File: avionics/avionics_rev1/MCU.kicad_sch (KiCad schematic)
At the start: 13 parts, among them U2 STM32G474RETx

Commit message: saving work before chat
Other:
- note added: "TODO: pins for SPI / I2C devices pins for buzzer / status LED(s) pins for pyro channels pins for battery monitoring / current draw determine if this needs a crystal or not (prolly) pins for USB connections pins for debug header"
- note removed: "TODO: pins for SPI / I2C devices pins for buzzer / status LED(s) pins for pyro channels pins for battery monitoring / current draw"
- moved on the sheet: C10, C11, C14, C6, C7, C8, C9, FB1

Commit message: working on sensors schematics
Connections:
- net VREF: no longer FB2.2, U2.28 (VREF+)
- new net: FB2.2, U2.28 (VREF+)
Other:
- note added: "TODO: determine pins for SPI / I2C devices determine pins for buzzer / status LED(s) determine pins for pyro channels determine pins for battery monitoring / current draw (find IC for current sensing) determine if this needs a crystal or not (probably) determine pins for USB connections determine pins for other telemetry IO setup a debug header / look into STlink find a flash memory chip and wire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"
- note removed: "TODO: pins for SPI / I2C devices pins for buzzer / status LED(s) pins for pyro channels pins for battery monitoring / current draw determine if this needs a crystal or not (prolly) pins for USB connections pins for debug header"
- moved on the sheet: BZ1, C14

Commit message: saving MCU work before using codex
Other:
- note added: "TODO: determine pins for SPI / I2C (if any) devices determine pins for buzzer / status LED(s) determine pins for pyro channels determine pins for battery monitoring / current draw (find IC for current sensing) determine if this needs a crystal or not (probably) determine pins for USB connections determine pins for other telemetry IO setup a debug header / look into STlink find a flash memory chip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"
- note removed: "TODO: determine pins for SPI / I2C devices determine pins for buzzer / status LED(s) determine pins for pyro channels determine pins for battery monitoring / current draw (find IC for current sensing) determine if this needs a crystal or not (probably) determine pins for USB connections determine pins for other telemetry IO setup a debug header / look into STlink find a flash memory chip and wire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"
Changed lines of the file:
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@@
 	(generator "eeschema")
 	(generator_version "10.0")
-	(paper "A4")
+	(paper "A3")
 	(text "Reference the Nucleo64 STM32G4 board\nfor this power layout"
 		(exclude_from_sim no)
@@
 		)
 	)
-	(text "TODO: \ndetermine pins for SPI / I2C devices\ndetermine pins for buzzer / status LED(s)\ndetermine pins for pyro channels\ndetermine pins for battery monitoring / \ncurrent draw (find IC for current sensing)\ndetermine if this needs a crystal or not (probably)\ndetermine pins for USB connections\ndetermine pins for other telemetry IO\nsetup a debug header / look into STlink\nfind a flash memory chip and wire it up"
+	(text "TODO: \ndetermine pins for SPI / I2C (if any) devices\ndetermine pins for buzzer / status LED(s)\ndetermine pins for pyro channels\ndetermine pins for battery monitoring / \ncurrent draw (find IC for current sensing)\ndetermine if this needs a crystal or not (probably)\ndetermine pins for USB connections\ndetermine pins for other telemetry IO\nsetup a debug header / look into STlink\nfind a flash memory chip and wire it up (needs to hold flight data)\nconnect existing flags to corresponding pins\nadd voltages/tolerances for capacitors/resistors"
 		(exclude_from_sim no)
-		(at 20.32 40.894 0)
+		(at 214.63 122.936 0)
 		(effects
 			(font

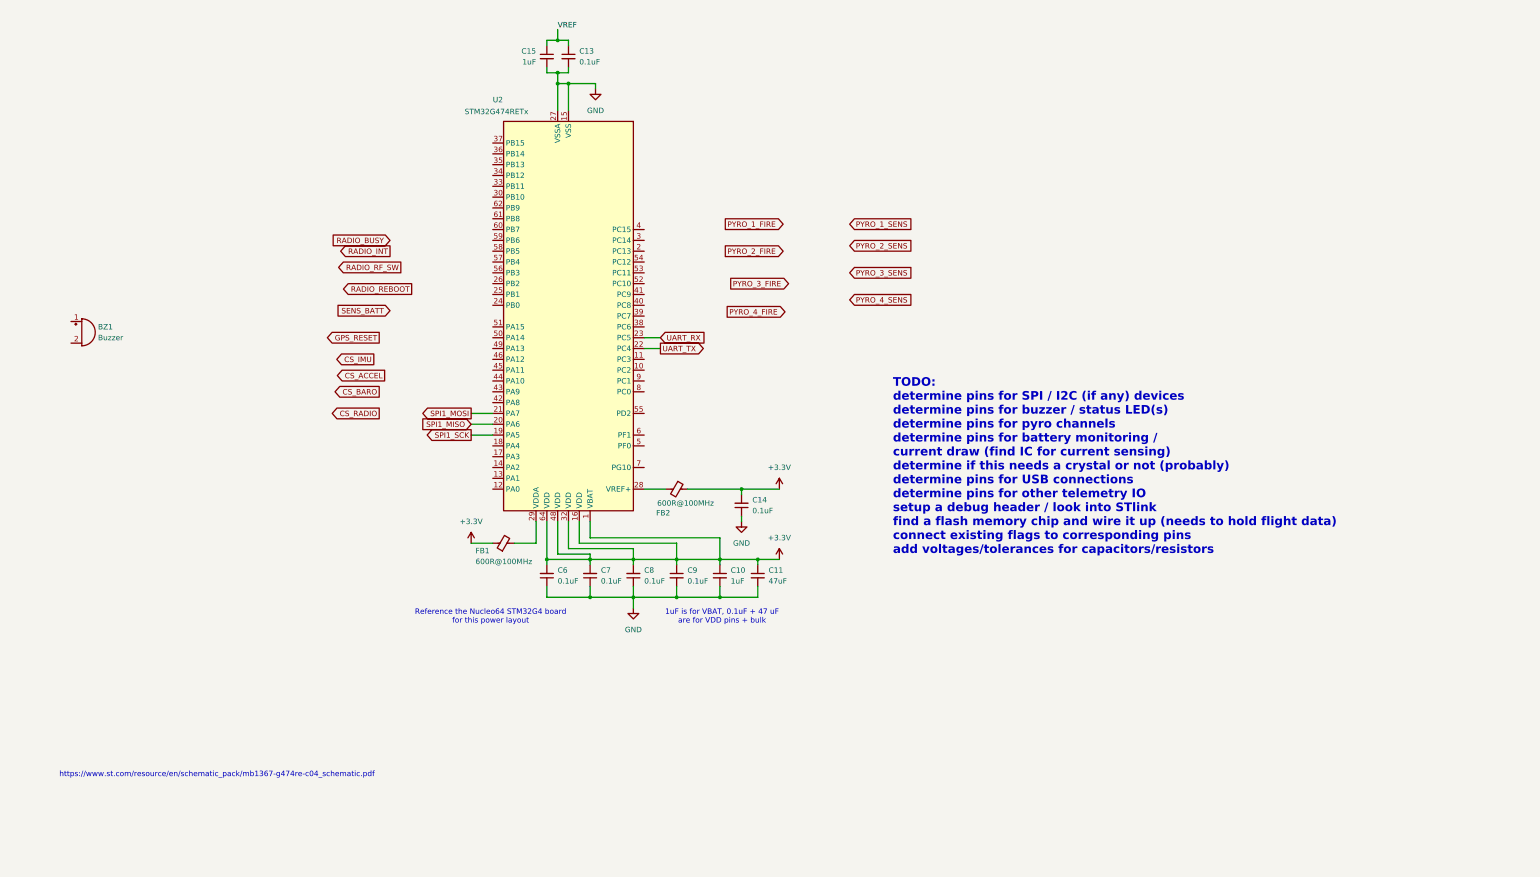
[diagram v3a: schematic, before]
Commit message: cleaned up schematics after codex work
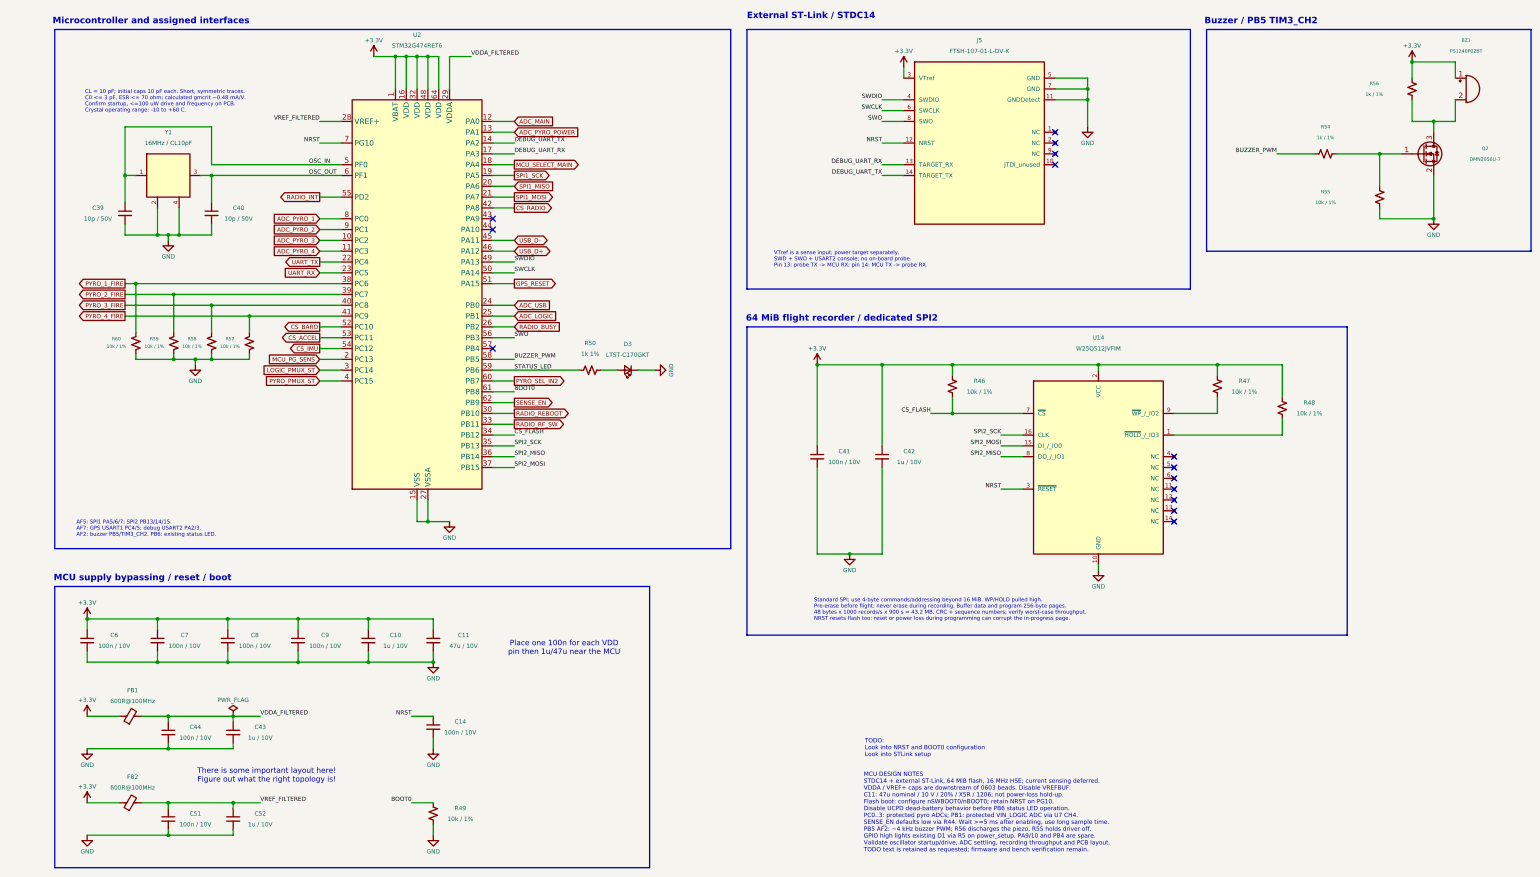
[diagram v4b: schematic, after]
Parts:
- removed BZ1: Buzzer, avionics_footprints:XDCR_PS1240P02BT, symbol Device:Buzzer
- removed C13: 0.1uF, Capacitor_SMD:C_0201_0603Metric, symbol Device:C_Small
- removed C15: 1uF, Capacitor_SMD:C_0201_0603Metric, symbol Device:C_Small
- removed FB2: 600R@100MHz, Capacitor_SMD:C_0201_0603Metric, symbol Device:FerriteBead_Small
- added BZ1: PS1240P02BT, avionics_footprints:XDCR_PS1240P02BT, symbol rocketry_library:PS1240P02BT
- added C39, C40: 10p / 50V, Capacitor_SMD:C_0402_1005Metric, symbol rocketry_library:C0402C100J5GACTU
- added C41, C44, C51: 100n / 10V, Capacitor_SMD:C_0402_1005Metric, symbol rocketry_library:GRM155R71A104KA01D
- added C42, C43, C52: 1u / 10V, Capacitor_SMD:C_0603_1608Metric, symbol rocketry_library:C1608X7R1A105K080AC
- added D3: LTST-C170GKT, avionics_footprints:LTST_C170GKT_0805, symbol Device:LED_Small
- added FB2: 600R@100MHz, Inductor_SMD:L_0603_1608Metric, symbol rocketry_library:BLM18AG601SN1D
- added J5: FTSH-107-01-L-DV-K, avionics_footprints:FTSH-107-01-L-DV-K_STDC14, symbol rocketry_library:FTSH-107-01-L-DV-K_STDC14
- added Q2: DMN2056U-7, avionics_footprints:DMN2056U_7_SOT23, symbol rocketry_library:DMN2056U-7
- added R46, R47, R48, R49, R55, R57, R58, R59, R60: 10k / 1%, Resistor_SMD:R_0402_1005Metric, symbol rocketry_library:RC0402FR-0710KL
- added R50: 1k 1%, Resistor_SMD:R_0402_1005Metri, symbol rocketry_library:RC0402FR-071KL
- added R54, R56: 1k / 1%, Resistor_SMD:R_0402_1005Metric, symbol rocketry_library:RC0402FR-071KL
- added U14: W25Q512JVFIM, avionics_footprints:W25Q512JVFIM_SOIC16W, symbol rocketry_library:W25Q512JVFIM
- added Y1: 16MHz / CL10pF, avionics_footprints:ABM8_3.2x2.5mm, symbol rocketry_library:ABM8-16.000MHZ-10-1-U-T
- C10: value 1uF -> 1u / 10V; footprint Capacitor_SMD:C_0201_0603Metric -> Capacitor_SMD:C_0603_1608Metric; symbol Device:C_Small -> rocketry_library:C1608X7R1A105K080AC; Dielectric (none) -> X7R; DigiKey (none) -> https://www.digikey.com/en/products/detail/tdk/C1608X7R1A10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; MPN (none) -> C1608X7R1A105K080AC; Tolerance (none) -> 10%; Voltage (none) -> 10V
- C11: value 47uF -> 47u / 10V; footprint Capacitor_SMD:C_0201_0603Metric -> Capacitor_SMD:C_1206_3216Metric; symbol Device:C_Small -> rocketry_library:C3216X5R1A476M160AB; Dielectric (none) -> X5R; DigiKey (none) -> https://www.digikey.com/en/products/detail/tdk/C3216X5R1A47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; MPN (none) -> C3216X5R1A476M160AB; Tolerance (none) -> 20%; Voltage (none) -> 10V
- C14, C6, C7, C8, C9: value 0.1uF -> 100n / 10V; footprint Capacitor_SMD:C_0201_0603Metric -> Capacitor_SMD:C_0402_1005Metric; symbol Device:C_Small -> rocketry_library:GRM155R71A104KA01D; Dielectric (none) -> X7R; DigiKey (none) -> https://www.digikey.com/en/products/detail/murata-electroni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; MPN (none) -> GRM155R71A104KA01D; Tolerance (none) -> 10%; Voltage (none) -> 10V
- FB1: footprint Capacitor_SMD:C_0201_0603Metric -> Inductor_SMD:L_0603_1608Metric; symbol Device:FerriteBead_Small -> rocketry_library:BLM18AG601SN1D; DigiKey (none) -> https://www.digikey.com/en/products/detail/murata-electroni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; Impedance tolerance (none) -> 25%; MPN (none) -> BLM18AG601SN1D
- U2: value STM32G474RETx -> STM32G474RET6; symbol MCU_ST_STM32G4:STM32G474RETx -> rocketry_library:STM32G474RET6
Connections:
- net +3.3V: now also C6.1, C7.1, C8.1, BZ1.1 (+), C41.1, C42.1, FB2.1, J5.3 (VTref), R46.1, R47.1, R48.1, R56.1, U14.2 (VCC); no longer C14.2, C6.2, C7.2, C8.2
- net CS_ACCEL: now also U2.53 (PC11)
- net CS_BARO: now also U2.52 (PC10)
- net CS_IMU: now also U2.54 (PC12)
- net CS_RADIO: now also U2.42 (PA8)
- net GND: now also C14.2, C6.2, C7.2, C8.2, C39.2, C40.2, C41.2, C42.2, C43.2, C44.2, C51.2, C52.2, D3.1 (K), J5.11 (GNDDetect), J5.5 (GND), J5.7 (GND), Q2.2 (S), R49.2, R55.2, R57.2, R58.2, R59.2, R60.2, U14.10 (GND), Y1.2 (CASE), Y1.4 (CASE); no longer C14.1, C6.1, C7.1, C8.1
- net GPS_RESET: now also U2.51 (PA15)
- net PYRO_1_FIRE: now also U2.38 (PC6), R60.1
- net PYRO_2_FIRE: now also U2.39 (PC7), R59.1
- net PYRO_3_FIRE: now also U2.40 (PC8), R58.1
- net PYRO_4_FIRE: now also U2.41 (PC9), R57.1
- net RADIO_BUSY: now also U2.26 (PB2)
- net RADIO_INT: now also U2.55 (PD2)
- net RADIO_REBOOT: now also U2.30 (PB10)
- net RADIO_RF_SW: now also U2.33 (PB11)
- net VDDA_FILTERED: now reaches FB1.2, U2.29 (VDDA)
- net VDDA_FILTERED: now also C43.1, C44.1
- net VREF_FILTERED: now reaches U2.28 (VREF+)
- net VREF_FILTERED: now also C51.1, C52.1, FB2.2
- net ADC_PYRO_3: now reaches U2.10 (PC2)
- net ADC_PYRO_4: now reaches U2.11 (PC3)
- net ADC_MAIN: now reaches U2.12 (PA0)
- net ADC_PYRO_POWER: now reaches U2.13 (PA1)
- net DEBUG_UART_TX: now reaches U2.14 (PA2)
- net DEBUG_UART_TX: now also J5.14 (TARGET_TX)
- net DEBUG_UART_RX: now reaches U2.17 (PA3)
- net DEBUG_UART_RX: now also J5.13 (TARGET_RX)
- net MCU_SELECT_MAIN: now reaches U2.18 (PA4)
- net MCU_PG_SENS: now reaches U2.2 (PC13)
- net ADC_USB: now reaches U2.24 (PB0)
- net ADC_LOGIC: now reaches U2.25 (PB1)
- net LOGIC_PMUX_ST: now reaches U2.3 (PC14)
- net CS_FLASH: now reaches U2.34 (PB12)
- net CS_FLASH: now also R46.2, U14.7 (~{CS})
- net SPI2_SCK: now reaches U2.35 (PB13)
- net SPI2_SCK: now also U14.16 (CLK)
- net SPI2_MISO: now reaches U2.36 (PB14)
- net SPI2_MISO: now also U14.8 (DO_/_IO1)
- net SPI2_MOSI: now reaches U2.37 (PB15)
- net SPI2_MOSI: now also U14.15 (DI_/_IO0)
- net PYRO_PMUX_ST: now reaches U2.4 (PC15)
- net USB_D-: now reaches U2.45 (PA11)
- net USB_D+: now reaches U2.46 (PA12)
- net SWDIO: now reaches U2.49 (PA13)
- net SWDIO: now also J5.4 (SWDIO)
- net OSC_IN: now reaches U2.5 (PF0)
- net OSC_IN: now also C39.1, Y1.1 (OSC1)
- net SWCLK: now reaches U2.50 (PA14)
- net SWCLK: now also J5.6 (SWCLK)
- net SWO: now reaches U2.56 (PB3)
- net SWO: now also J5.8 (SWO)
- net BUZZER_PWM: now reaches U2.58 (PB5)
- net BUZZER_PWM: now also R54.1
- net STATUS_LED: now reaches U2.59 (PB6)
- net STATUS_LED: now also R50.2
- net OSC_OUT: now reaches U2.6 (PF1)
- net OSC_OUT: now also C40.1, Y1.3 (OSC2)
- net PYRO_SEL_IN2: now reaches U2.60 (PB7)
- net BOOT0: now reaches U2.61 (PB8)
- net BOOT0: now also R49.1
- net SENSE_EN: now reaches U2.62 (PB9)
- net NRST: now reaches U2.7 (PG10)
- net NRST: now also C14.1, J5.12 (NRST), U14.3 (~{RESET})
- net ADC_PYRO_1: now reaches U2.8 (PC0)
- net ADC_PYRO_2: now reaches U2.9 (PC1)
- new net: Q2.1 (G), R54.2, R55.1
- new net: BZ1.2 (-), Q2.3 (D), R56.2
- new net: R48.2, U14.1 (~{HOLD}_/_IO3)
- new net: R47.2, U14.9 (~{WP}_/_IO2)
- new net: D3.2 (A), R50.1
- no-connect marks 0 -> 14
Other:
- note added: "64 MiB flight recorder / dedicated SPI2"
- note added: "AF5: SPI1 PA5/6/7; SPI2 PB13/14/15. AF7: GPS USART1 PC4/5; debug USART2 PA2/3. AF2: buzzer PB5/TIM3_CH2. PB6: existing status LED."
- note added: "Buzzer / PB5 TIM3_CH2"
- note added: "CL = 10 pF; initial caps 10 pF each. Short, symmetric traces. C0 <= 3 pF, ESR <= 70 ohm; calculated gmcrit ~0.48 mA/V. Confirm startup, <=100 uW drive and frequency on PCB. Crystal operating range: -10 to +60 C."
- note added: "External ST-Link / STDC14"
- note added: "MCU DESIGN NOTES STDC14 + external ST-Link, 64 MiB flash, 16 MHz HSE; current sensing deferred. VDDA / VREF+ caps are downstream of 0603 beads. Disable VREFBUF. C11: 47u nominal / 10 V / 20% / X5R / 1206; not power-loss hold-up. Flash boot: configure nSWBOOT0/nBOOT0; retain NRST on PG10. Disable UCPD dead-battery behavior before PB6 status LED operation. PC0..3: protected pyro ADCs; PB1: protecte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"
- note added: "MCU supply bypassing / reset / boot"
- note added: "Microcontroller and assigned interfaces"
- note added: "Place one 100n for each VDD pin then 1u/47u near the MCU"
- note added: "Standard SPI; use 4-byte commands/addressing beyond 16 MiB. WP/HOLD pulled high. Pre-erase before flight; never erase during recording. Buffer data and program 256-byte pages. 48 bytes x 1000 records/s x 900 s = 43.2 MB. CRC + sequence numbers; verify worst-case throughput. NRST resets flash too: reset or power loss during programming can corrupt the in-progress page."
- note added: "TODO: Look into NRST and BOOT0 configuration Look into STLink setup"
- note added: "There is some important layout here! Figure out what the right topology is!"
- note added: "VTref is a sense input; power target separately. SWD + SWO + USART2 console; no on-board probe. Pin 13: probe TX -> MCU RX; pin 14: MCU TX -> probe RX."
- note removed: "1uF is for VBAT, 0.1uF + 47 uF are for VDD pins + bulk"
- note removed: "Reference the Nucleo64 STM32G4 board for this power layout"
- note removed: "TODO: determine pins for SPI / I2C (if any) devices determine pins for buzzer / status LED(s) determine pins for pyro channels determine pins for battery monitoring / current draw (find IC for current sensing) determine if this needs a crystal or not (probably) determine pins for USB connections determine pins for other telemetry IO setup a debug header / look into STlink find a flash memory chip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"
- note removed: "https://www.st.com/resource/en/schematic_pack/mb1367-g474re-c04_schematic.pdf"
- moved on the sheet: C10, C11, C14, C6, C7, C8, C9, FB1, U2

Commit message: saving MCU work before using codex
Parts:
- added TP10, TP11, TP12, TP13: TestPoint, symbol Connector:TestPoint
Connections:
- net PYRO_1_FIRE: now also TP10.1
- net PYRO_2_FIRE: now also TP11.1
- net PYRO_3_FIRE: now also TP12.1
- net PYRO_4_FIRE: now also TP13.1
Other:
- moved on the sheet: C39, C40, R57, R58, R59, R60, Y1

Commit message: fixed ERC errors
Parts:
- C10, C42, C43, C52: value 1u / 10V -> 1u
- C11: value 47u / 10V -> 47u
- C14, C41, C44, C51, C6, C7, C8, C9: value 100n / 10V -> 100n
- C39, C40: value 10p / 50V -> 10p
- J5: MPN FTSH-107-01-L-DV-K_STDC14 -> FTSH-107-01-L-DV-K
- R46, R47, R48, R49, R55, R57, R58, R59, R60: value 10k / 1% -> 10k
- R50: value 1k 1% -> 1k; footprint Resistor_SMD:R_0402_1005Metri -> Resistor_SMD:R_0402_1005Metric
- R54, R56: value 1k / 1% -> 1k
- TP10, TP11, TP12, TP13: footprint (none) -> TestPoint:TestPoint_Pad_D1.0mm; now left out of the parts list
- U2: DigiKey (none) -> https://www.digikey.com/en/products/detail/stmicroelectroni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; MPN (none) -> STM32G474RET6; Manufacturer (none) -> STMicroelectronics
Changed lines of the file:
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@@
 		(body_style 1)
 		(exclude_from_sim no)
-		(in_bom yes)
+		(in_bom no)
 		(on_board yes)
 		(in_pos_files yes)
@@
 			)
 		)
-		(property "Footprint" ""
+		(property "Footprint" "TestPoint:TestPoint_Pad_D1.0mm"
 			(at 55.88 88.9 0)
 			(hide yes)
@@
 			)
 		)
-		(property "Description" "test point"
+		(property "Description" "Bare PCB copper test pad, no purchased component"
 			(at 60.96 88.9 0)
 			(hide yes)
@@
 			)
 		)
-		(property "Value" "1u / 10V"
+		(property "Value" "1u"
 			(at 97.79 165.1 0)
 			(show_name no)
@@
 			)
 		)
-		(property "Value" "100n / 10V"
+		(property "Value" "100n"
 			(at 203.2 121.92 0)
 			(show_name no)
@@
 			)
 		)
-		(property "Value" "1k / 1%"
+		(property "Value" "1k"
 			(at 327.66 35.56 0)
 			(show_name no)
@@
 			)
 		)
-		(property "Value" "10k / 1%"
+		(property "Value" "10k"
 			(at 312.42 110.49 0)
 			(show_name no)
@@
 			)
 		)
-		(property "Value" "10p / 50V"
+		(property "Value" "10p"
 			(at 59.69 58.42 0)
 			(show_name no)
@@
 			)
 		)
-		(property "Value" "100n / 10V"
+		(property "Value" "100n"
 			(at 31.75 165.1 0)
 			(show_name no)
@@
 		(body_style 1)
 		(exclude_from_sim no)
-		(in_bom yes)
+		(in_bom no)
 		(on_board yes)
 		(in_pos_files yes)
@@
 			)
 		)
-		(property "Footprint" ""
+		(property "Footprint" "TestPoint:TestPoint_Pad_D1.0mm"
 			(at 46.99 88.9 0)
 			(hide yes)
@@
 			)
 		)
-		(property "Description" "test point"
+		(property "Description" "Bare PCB copper test pad, no purchased component"
 			(at 52.07 88.9 0)
 			(hide yes)
@@
 			)
 		)
-		(property "Value" "100n / 10V"
+		(property "Value" "100n"
 			(at 50.8 207.01 0)
 			(show_name no)
@@
 			)
 		)
-		(property "Value" "100n / 10V"
+		(property "Value" "100n"
 			(at 48.26 165.1 0)
 			(show_name no)
@@
 			)
 		)
-		(property "Value" "1u / 10V"
+		(property "Value" "1u"
 			(at 218.44 121.92 0)
 			(show_name no)
@@
 			)
 		)
-		(property "Value" "10k / 1%"
+		(property "Value" "10k"
 			(at 41.148 102.362 0)
 			(show_name no)
@@
 			)
 		)
-		(property "Value" "1k / 1%"
+		(property "Value" "1k"
 			(at 316.23 45.72 90)
 			(show_name no)
@@
 			)
 		)
-		(property "Value" "100n / 10V"
+		(property "Value" "100n"
 			(at 50.8 186.69 0)
 			(show_name no)
@@
 			)
 		)
-		(property "Value" "10k / 1%"
+		(property "Value" "10k"
 			(at 113.03 205.74 0)
 			(show_name no)
@@
 			)
 		)
-		(property "Value" "10k / 1%"
+		(property "Value" "10k"
 			(at 234.95 105.41 0)
 			(show_name no)
@@
 			)
 		)
-		(property "Value" "10k / 1%"
+		(property "Value" "10k"
 			(at 32.258 102.362 0)
 			(show_name no)
@@
 			)
 		)
-		(property "Value" "1u / 10V"
+		(property "Value" "1u"
 			(at 66.04 207.01 0)
 			(show_name no)
@@
 			)
 		)
-		(property "Value" "10k / 1%"
+		(property "Value" "10k"
 			(at 50.038 102.362 0)
 			(show_name no)
@@
 			)
 		)
-		(property "Value" "1u / 10V"
+		(property "Value" "1u"
 			(at 66.04 186.69 0)
 			(show_name no)
@@
 			)
 		)
-		(property "Value" "1k 1%"
+		(property "Value" "1k"
 			(at 143.51 96.52 90)
 			(show_name no)
@@
 			)
 		)
-		(property "Footprint" "Resistor_SMD:R_0402_1005Metri"
+		(property "Footprint" "Resistor_SMD:R_0402_1005Metric"
 			(at 143.51 100.33 0)
 			(hide yes)
@@
 			)
 		)
-		(property "Value" "47u / 10V"
+		(property "Value" "47u"
 			(at 113.792 165.1 0)
 			(show_name no)
@@
 			)
 		)
-		(property "Value" "100n / 10V"
+		(property "Value" "100n"
 			(at 113.03 185.42 0)
 			(show_name no)
@@
 			)
 		)
-		(property "Value" "10k / 1%"
+		(property "Value" "10k"
 			(at 297.18 105.41 0)
 			(show_name no)
@@
 			)
 		)
-		(property "MPN" "FTSH-107-01-L-DV-K_STDC14"
+		(property "MPN" "FTSH-107-01-L-DV-K"
 			(at 234.95 46.99 0)
 			(hide yes)
@@
 			)
 		)
-		(property "Value" "10k / 1%"
+		(property "Value" "10k"
 			(at 316.23 60.96 0)
 			(show_name no)
@@
 			)
 		)
-		(property "Value" "100n / 10V"
+		(property "Value" "100n"
 			(at 81.28 165.1 0)
 			(show_name no)
@@
 			)
 		)
+		(property "MPN" "STM32G474RET6"
+			(at 0 0 0)
+			(hide yes)
+			(show_name no)
+			(do_not_autoplace no)
+			(effects
+				(font
+					(size 1 1)
+				)
+			)
+		)
+		(property "Manufacturer" "STMicroelectronics"
+			(at 0 0 0)
+			(hide yes)
+			(show_name no)
+			(do_not_autoplace no)
+			(effects
+				(font
+					(size 1 1)
+				)
+			)
+		)
+		(property "DigiKey" "https://www.digikey.com/en/products/detail/stmicroelectronics/STM32G474RET6/10326780"
+			(at 0 0 0)
+			(hide yes)
+			(show_name no)
+			(do_not_autoplace no)
+			(effects
+				(font
+					(size 1 1)
+				)
+			)
+		)
 		(pin "5"
 		)
@@
 		(body_style 1)
 		(exclude_from_sim no)
-		(in_bom yes)
+		(in_bom no)
 		(on_board yes)
 		(in_pos_files yes)
@@
 			)
 		)
-		(property "Footprint" ""
+		(property "Footprint" "TestPoint:TestPoint_Pad_D1.0mm"
 			(at 29.21 88.9 0)
 			(hide yes)
@@
 			)
 		)
-		(property "Description" "test point"
+		(property "Description" "Bare PCB copper test pad, no purchased component"
 			(at 34.29 88.9 0)
 			(hide yes)
@@
 			)
 		)
-		(property "Value" "10k / 1%"
+		(property "Value" "10k"
 			(at 58.928 102.362 0)
 			(show_name no)
@@
 			)
 		)
-		(property "Value" "100n / 10V"
+		(property "Value" "100n"
 			(at 64.77 165.1 0)
 			(show_name no)
@@
 			)
 		)
-		(property "Value" "10p / 50V"
+		(property "Value" "10p"
 			(at 26.67 58.42 0)
 			(show_name no)
@@
 		(body_style 1)
 		(exclude_from_sim no)
-		(in_bom yes)
+		(in_bom no)
 		(on_board yes)
 		(in_pos_files yes)
@@
 			)
 		)
-		(property "Footprint" ""
+		(property "Footprint" "TestPoint:TestPoint_Pad_D1.0mm"
 			(at 38.1 88.9 0)
 			(hide yes)
@@
 			)
 		)
-		(property "Description" "test point"
+		(property "Description" "Bare PCB copper test pad, no purchased component"
 			(at 43.18 88.9 0)
 			(hide yes)
